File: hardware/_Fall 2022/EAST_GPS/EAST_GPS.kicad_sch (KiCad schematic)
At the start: 3 parts, among them J1 Conn_02x08_Odd_Even, U1 GPS-14414, U2 RFM69HCW_Breakout

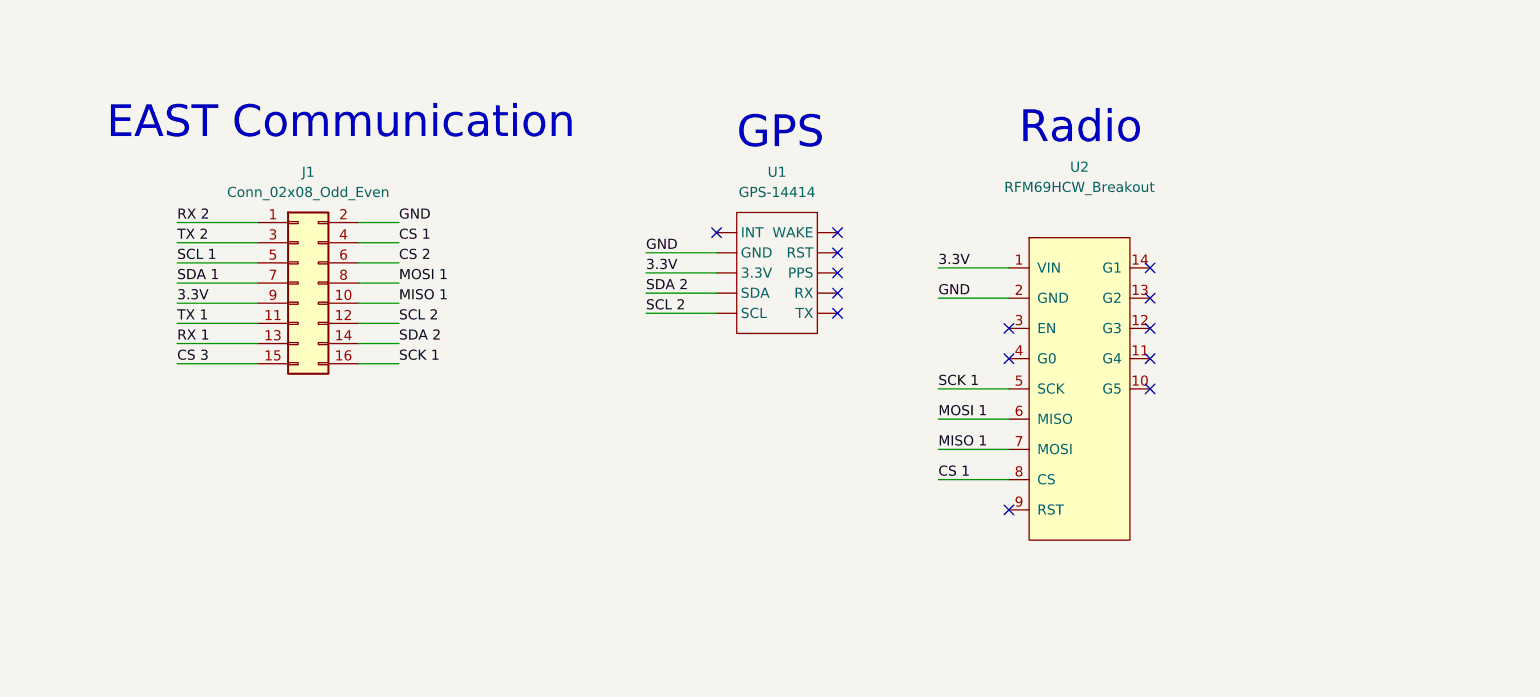
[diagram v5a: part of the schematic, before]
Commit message: Completed EAST Teensy board, confused at GPS board
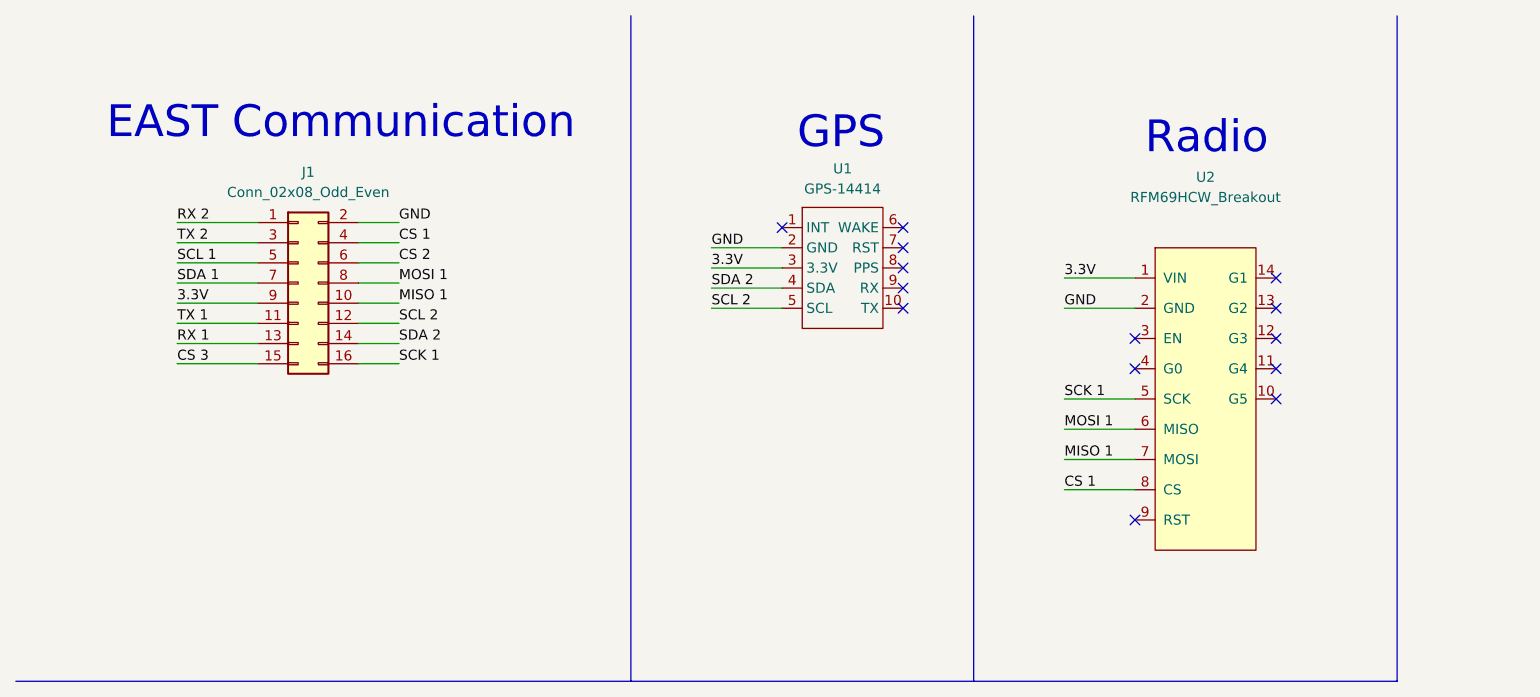
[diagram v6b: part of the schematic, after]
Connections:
- net 3.3V: now also U1.3 (3.3V); no longer U1. (WAKE)
- net GND: now also U1.2 (GND); no longer U1. (WAKE)
- net SCL 2: now also U1.5 (SCL); no longer U1. (WAKE)
- net SDA 2: now also U1.4 (SDA); no longer U1. (WAKE)
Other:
- moved on the sheet: U2
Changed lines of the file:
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@@
 (kicad_sch (version 20211123) (generator eeschema)
   (paper "A4")
-  (no_connect (at 114.935 40.005))
-  (no_connect (at 114.935 42.545))
-  (no_connect (at 114.935 45.085))
-  (no_connect (at 114.935 47.625))
-  (no_connect (at 114.935 50.165))
+  (no_connect (at 123.19 39.37))
+  (no_connect (at 123.19 41.91))
+  (no_connect (at 123.19 44.45))
+  (no_connect (at 123.19 46.99))
+  (no_connect (at 123.19 49.53))
   (no_connect (at 284.48 58.42))
-  (no_connect (at 99.695 40.005))
-  (no_connect (at 154.305 44.45))
-  (no_connect (at 136.525 52.07))
-  (no_connect (at 136.525 55.88))
-  (no_connect (at 154.305 59.69))
-  (no_connect (at 154.305 55.88))
-  (no_connect (at 154.305 52.07))
-  (no_connect (at 154.305 48.26))
-  (no_connect (at 136.525 74.93))
+  (no_connect (at 107.95 39.37))
+  (no_connect (at 170.18 45.72))
+  (no_connect (at 152.4 53.34))
+  (no_connect (at 152.4 57.15))
+  (no_connect (at 170.18 60.96))
+  (no_connect (at 170.18 57.15))
+  (no_connect (at 170.18 53.34))
+  (no_connect (at 170.18 49.53))
+  (no_connect (at 152.4 76.2))
   (wire (pts (xy 54.61 48.895) (xy 59.69 48.895))
     (stroke (width 0) (type default) (color 0 0 0 0))
@@
     (stroke (width 0) (type default) (color 0 0 0 0))
   )
-  (wire (pts (xy 127.635 44.45) (xy 136.525 44.45))
-    (stroke (width 0) (type default) (color 0 0 0 0))
-  )
-  (wire (pts (xy 90.805 45.085) (xy 99.695 45.085))
+  (wire (pts (xy 143.51 45.72) (xy 152.4 45.72))
+    (stroke (width 0) (type default) (color 0 0 0 0))
+  )
+  (wire (pts (xy 99.06 44.45) (xy 107.95 44.45))
     (stroke (width 0) (type default) (color 0 0 0 0))
   )
@@
     (stroke (width 0) (type default) (color 0 0 0 0))
   )
-  (wire (pts (xy 90.805 42.545) (xy 99.695 42.545))
+  (wire (pts (xy 99.06 41.91) (xy 107.95 41.91))
     (stroke (width 0) (type default) (color 0 0 0 0))
   )
@@
     (stroke (width 0) (type default) (color 0 0 0 0))
   )
-  (wire (pts (xy 90.805 50.165) (xy 99.695 50.165))
-    (stroke (width 0) (type default) (color 0 0 0 0))
-  )
-  (wire (pts (xy 127.635 48.26) (xy 136.525 48.26))
-    (stroke (width 0) (type default) (color 0 0 0 0))
-  )
-  (wire (pts (xy 127.635 71.12) (xy 136.525 71.12))
+  (wire (pts (xy 99.06 49.53) (xy 107.95 49.53))
+    (stroke (width 0) (type default) (color 0 0 0 0))
+  )
+  (wire (pts (xy 143.51 49.53) (xy 152.4 49.53))
+    (stroke (width 0) (type default) (color 0 0 0 0))
+  )
+  (wire (pts (xy 143.51 72.39) (xy 152.4 72.39))
+    (stroke (width 0) (type default) (color 0 0 0 0))
+  )
+  (polyline (pts (xy 185.42 12.7) (xy 185.42 96.52))
+    (stroke (width 0) (type default) (color 0 0 0 0))
+  )
+  (polyline (pts (xy 132.08 12.7) (xy 132.08 96.52))
     (stroke (width 0) (type default) (color 0 0 0 0))
   )
@@
     (stroke (width 0) (type default) (color 0 0 0 0))
   )
-  (wire (pts (xy 127.635 63.5) (xy 136.525 63.5))
+  (polyline (pts (xy 88.9 12.7) (xy 88.9 96.52))
+    (stroke (width 0) (type default) (color 0 0 0 0))
+  )
+  (wire (pts (xy 143.51 64.77) (xy 152.4 64.77))
     (stroke (width 0) (type default) (color 0 0 0 0))
   )
@@
     (stroke (width 0) (type default) (color 0 0 0 0))
   )
-  (wire (pts (xy 90.805 47.625) (xy 99.695 47.625))
+  (wire (pts (xy 99.06 46.99) (xy 107.95 46.99))
     (stroke (width 0) (type default) (color 0 0 0 0))
   )
@@
     (stroke (width 0) (type default) (color 0 0 0 0))
   )
-  (wire (pts (xy 127.635 59.69) (xy 136.525 59.69))
+  (wire (pts (xy 143.51 60.96) (xy 152.4 60.96))
     (stroke (width 0) (type default) (color 0 0 0 0))
   )
@@
     (stroke (width 0) (type default) (color 0 0 0 0))
   )
-  (wire (pts (xy 127.635 67.31) (xy 136.525 67.31))
+  (polyline (pts (xy 11.43 96.52) (xy 185.42 96.52))
+    (stroke (width 0) (type default) (color 0 0 0 0))
+  )
+  (wire (pts (xy 143.51 68.58) (xy 152.4 68.58))
     (stroke (width 0) (type default) (color 0 0 0 0))
   )
@@
     (effects (font (size 4 4)) (justify left bottom))
   )
-  (text "Radio" (at 137.795 29.21 0)
+  (text "Radio" (at 153.67 30.48 0)
     (effects (font (size 4 4)) (justify left bottom))
   )
-  (text "GPS" (at 102.235 29.845 0)
+  (text "GPS" (at 109.855 29.845 0)
     (effects (font (size 4 4)) (justify left bottom))
   )
@@
     (effects (font (size 1.27 1.27)) (justify left bottom))
   )
-  (label "MISO 1" (at 127.635 67.31 0)
-    (effects (font (size 1.27 1.27)) (justify left bottom))
-  )
-  (label "3.3V" (at 90.805 45.085 0)
+  (label "MISO 1" (at 143.51 68.58 0)
+    (effects (font (size 1.27 1.27)) (justify left bottom))
+  )
+  (label "3.3V" (at 99.06 44.45 0)
     (effects (font (size 1.27 1.27)) (justify left bottom))
   )
@@
     (effects (font (size 1.27 1.27)) (justify left bottom))
   )
-  (label "MOSI 1" (at 127.635 63.5 0)
-    (effects (font (size 1.27 1.27)) (justify left bottom))
-  )
-  (label "GND" (at 90.805 42.545 0)
+  (label "MOSI 1" (at 143.51 64.77 0)
+    (effects (font (size 1.27 1.27)) (justify left bottom))
+  )
+  (label "GND" (at 99.06 41.91 0)
     (effects (font (size 1.27 1.27)) (justify left bottom))
   )
@@
     (effects (font (size 1.27 1.27)) (justify left bottom))
   )
-  (label "SDA 2" (at 90.805 47.625 0)
+  (label "SDA 2" (at 99.06 46.99 0)
     (effects (font (size 1.27 1.27)) (justify left bottom))
   )
@@
     (effects (font (size 1.27 1.27)) (justify left bottom))
   )
-  (label "SCL 2" (at 90.805 50.165 0)
+  (label "SCL 2" (at 99.06 49.53 0)
     (effects (font (size 1.27 1.27)) (justify left bottom))
   )
@@
     (effects (font (size 1.27 1.27)) (justify left bottom))
   )
-  (label "CS 1" (at 127.635 71.12 0)
+  (label "CS 1" (at 143.51 72.39 0)
     (effects (font (size 1.27 1.27)) (justify left bottom))
   )
@@
     (effects (font (size 1.27 1.27)) (justify left bottom))
   )
-  (label "SCK 1" (at 127.635 59.69 0)
-    (effects (font (size 1.27 1.27)) (justify left bottom))
-  )
-  (label "3.3V" (at 127.635 44.45 0)
-    (effects (font (size 1.27 1.27)) (justify left bottom))
-  )
-  (label "GND" (at 127.635 48.26 0)
-    (effects (font (size 1.27 1.27)) (justify left bottom))
-  )
-  (symbol (lib_id "GPS:GPS-14414") (at 107.315 41.275 0) (unit 1)
+  (label "SCK 1" (at 143.51 60.96 0)
+    (effects (font (size 1.27 1.27)) (justify left bottom))
+  )
+  (label "3.3V" (at 143.51 45.72 0)
+    (effects (font (size 1.27 1.27)) (justify left bottom))
+  )
+  (label "GND" (at 143.51 49.53 0)
+    (effects (font (size 1.27 1.27)) (justify left bottom))
+  )
+  (symbol (lib_name "GPS-14414_1") (lib_id "GPS:GPS-14414") (at 115.57 40.64 0) (unit 1)
     (in_bom yes) (on_board yes) (fields_autoplaced)
-    (property "Reference" "U1" (id 0) (at 107.315 32.385 0))
-    (property "Value" "GPS-14414" (id 1) (at 107.315 34.925 0))
-    (property "Footprint" "GPS_layout:GPS-14414" (id 2) (at 107.315 41.275 0)
-      (effects (font (size 1.27 1.27)) hide)
-    )
-    (property "Datasheet" "" (id 3) (at 107.315 41.275 0)
-      (effects (font (size 1.27 1.27)) hide)
-    )
-    (pin "")
-    (pin "")
-    (pin "")
-    (pin "")
-    (pin "")
-    (pin "")
-    (pin "")
-    (pin "")
-    (pin "")
-    (pin "")
+    (property "Reference" "U1" (id 0) (at 115.57 31.956 0))
+    (property "Value" "GPS-14414" (id 1) (at 115.57 34.496 0))
+    (property "Footprint" "GPS_layout:GPS-14414" (id 2) (at 115.57 40.64 0)
+      (effects (font (size 1.27 1.27)) hide)
+    )
+    (property "Datasheet" "" (id 3) (at 115.57 40.64 0)
+      (effects (font (size 1.27 1.27)) hide)
+    )
+    (pin "1")
+    (pin "10")
+    (pin "2")
+    (pin "3")
+    (pin "4")
+    (pin "5")
+    (pin "6")
+    (pin "7")
+    (pin "8")
+    (pin "9")
   )
   (symbol (lib_id "Connector_Generic:Conn_02x08_Odd_Even") (at 46.99 46.355 0) (unit 1)
@@
     (pin "9")
   )
-  (symbol (lib_id "sensors:RFM69HCW_Breakout") (at 145.415 59.69 0) (unit 1)
+  (symbol (lib_id "sensors:RFM69HCW_Breakout") (at 161.29 60.96 0) (unit 1)
     (in_bom yes) (on_board yes) (fields_autoplaced)
-    (property "Reference" "U2" (id 0) (at 145.415 31.75 0))
-    (property "Value" "RFM69HCW_Breakout" (id 1) (at 145.415 34.29 0))
-    (property "Footprint" "Sensors:RFM69HCW_Breakout" (id 2) (at 141.605 39.37 0)
-      (effects (font (size 1.27 1.27)) hide)
-    )
-    (property "Datasheet" "" (id 3) (at 141.605 39.37 0)
+    (property "Reference" "U2" (id 0) (at 161.29 33.02 0))
+    (property "Value" "RFM69HCW_Breakout" (id 1) (at 161.29 35.56 0))
+    (property "Footprint" "Sensors:RFM69HCW_Breakout" (id 2) (at 157.48 40.64 0)
+      (effects (font (size 1.27 1.27)) hide)
+    )
+    (property "Datasheet" "" (id 3) (at 157.48 40.64 0)
       (effects (font (size 1.27 1.27)) hide)
     )
@@
       (reference "J1") (unit 1) (value "Conn_02x08_Odd_Even") (footprint "Connector_PinHeader_2.54mm:PinHeader_2x08_P2.54mm_Vertical")
     )
-    (path "/9267fdf1-f492-4ff5-8933-e2543b0cd96f"
+    (path "/c0880254-2ff2-43cf-b1b0-7c575ba139b4"
       (reference "U1") (unit 1) (value "GPS-14414") (footprint "GPS_layout:GPS-14414")
     )

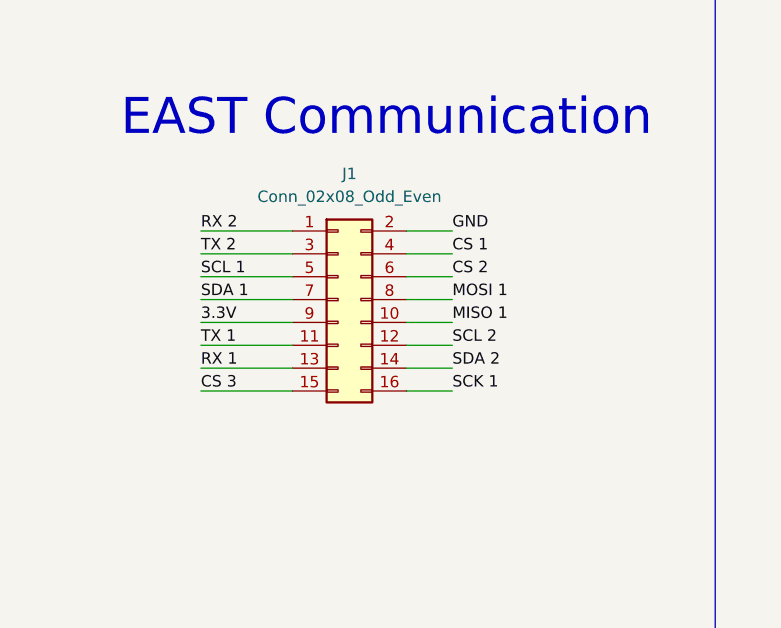
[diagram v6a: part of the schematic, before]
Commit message: Update EAST connectors
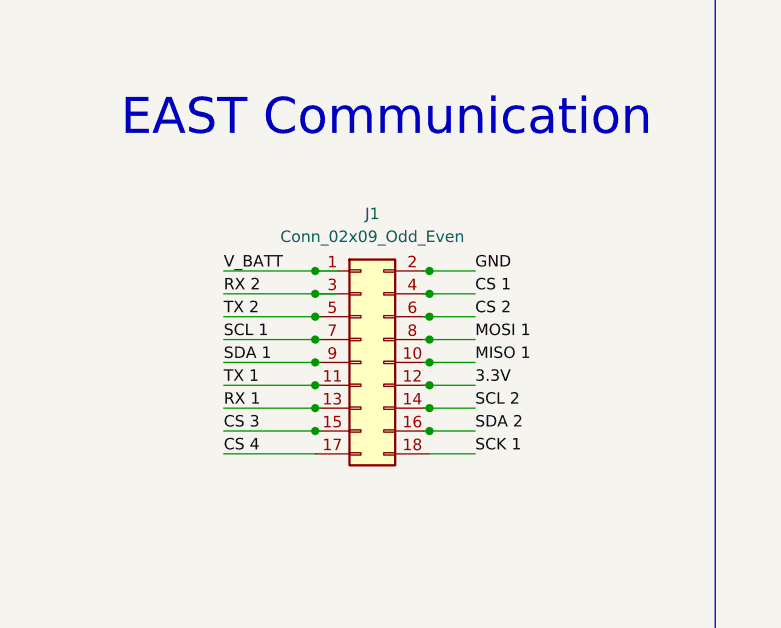
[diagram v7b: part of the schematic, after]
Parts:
- removed J1: Conn_02x08_Odd_Even, Connector_PinHeader_2.54mm:PinHeader_2x08_P2.54mm_Vertical, symbol Connector_Generic:Conn_02x08_Odd_Even
- added J1: Conn_02x09_Odd_Even, Connector_PinHeader_2.54mm:PinHeader_2x09_P2.54mm_Vertical, symbol Connector_Generic:Conn_02x09_Odd_Even
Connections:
- net 3.3V: now also J1.12 (Pin_12)
- net CS 1: now also J1.4 (Pin_4)
- net CS 2: now also J1.6 (Pin_6)
- net CS 3: now also J1.15 (Pin_15)
- net GND: now also J1.2 (Pin_2)
- net MISO 1: now also J1.10 (Pin_10)
- net MOSI 1: now also J1.8 (Pin_8)
- net RX 1: now also J1.13 (Pin_13)
- net RX 2: now also J1.3 (Pin_3)
- net SCK 1: now also J1.18 (Pin_18)
- net SCL 1: now also J1.7 (Pin_7)
- net SCL 2: now also J1.14 (Pin_14)
- net SDA 1: now also J1.9 (Pin_9)
- net SDA 2: now also J1.16 (Pin_16)
- net TX 1: now also J1.11 (Pin_11)
- net TX 2: now also J1.5 (Pin_5)
- new net CS 4: J1.17 (Pin_17)
- new net V_BATT: J1.1 (Pin_1)

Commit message: pcb fixes
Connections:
- net MISO 1: now also U2.6 (MISO); no longer U2.7 (MOSI)
- net MOSI 1: now also U2.7 (MOSI); no longer U2.6 (MISO)
- net RX 2: now also U2.4 (G0)
- net TX 2: now also U2.9 (RST)
- no-connect marks 15 -> 13
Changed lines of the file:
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@@
   (no_connect (at 170.18 45.72))
   (no_connect (at 152.4 53.34))
-  (no_connect (at 152.4 57.15))
   (no_connect (at 170.18 60.96))
   (no_connect (at 170.18 57.15))
   (no_connect (at 170.18 53.34))
   (no_connect (at 170.18 49.53))
-  (no_connect (at 152.4 76.2))
   (wire (pts (xy 57.15 50.8) (xy 62.23 50.8))
     (stroke (width 0) (type default) (color 0 0 0 0))
@@
     (stroke (width 0) (type default) (color 0 0 0 0))
   )
+  (wire (pts (xy 143.51 76.2) (xy 152.4 76.2))
+    (stroke (width 0) (type default) (color 0 0 0 0))
+  )
   (wire (pts (xy 34.29 53.34) (xy 44.45 53.34))
     (stroke (width 0) (type default) (color 0 0 0 0))
@@
   )
   (wire (pts (xy 34.29 63.5) (xy 44.45 63.5))
+    (stroke (width 0) (type default) (color 0 0 0 0))
+  )
+  (wire (pts (xy 143.51 57.15) (xy 152.4 57.15))
     (stroke (width 0) (type default) (color 0 0 0 0))
   )
@@
     (effects (font (size 1.27 1.27)) (justify left bottom))
   )
-  (label "MISO 1" (at 143.51 68.58 0)
+  (label "MOSI 1" (at 143.51 68.58 0)
     (effects (font (size 1.27 1.27)) (justify left bottom))
   )
@@
     (effects (font (size 1.27 1.27)) (justify left bottom))
   )
-  (label "MOSI 1" (at 143.51 64.77 0)
+  (label "MISO 1" (at 143.51 64.77 0)
     (effects (font (size 1.27 1.27)) (justify left bottom))
   )
@@
     (effects (font (size 1.27 1.27)) (justify left bottom))
   )
+  (label "TX 2" (at 143.51 76.2 0)
+    (effects (font (size 1.27 1.27)) (justify left bottom))
+  )
   (label "SDA 2" (at 99.06 46.99 0)
     (effects (font (size 1.27 1.27)) (justify left bottom))
@@
     (effects (font (size 1.27 1.27)) (justify left bottom))
   )
+  (label "RX 2" (at 143.51 57.15 0)
+    (effects (font (size 1.27 1.27)) (justify left bottom))
+  )
